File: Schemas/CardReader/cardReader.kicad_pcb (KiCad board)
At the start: 2 copper layers, 50.2 x 56.5 mm, 29 parts, among them P1 PWR, P2 DATA, Q1 BC817-40, U1 74HC165

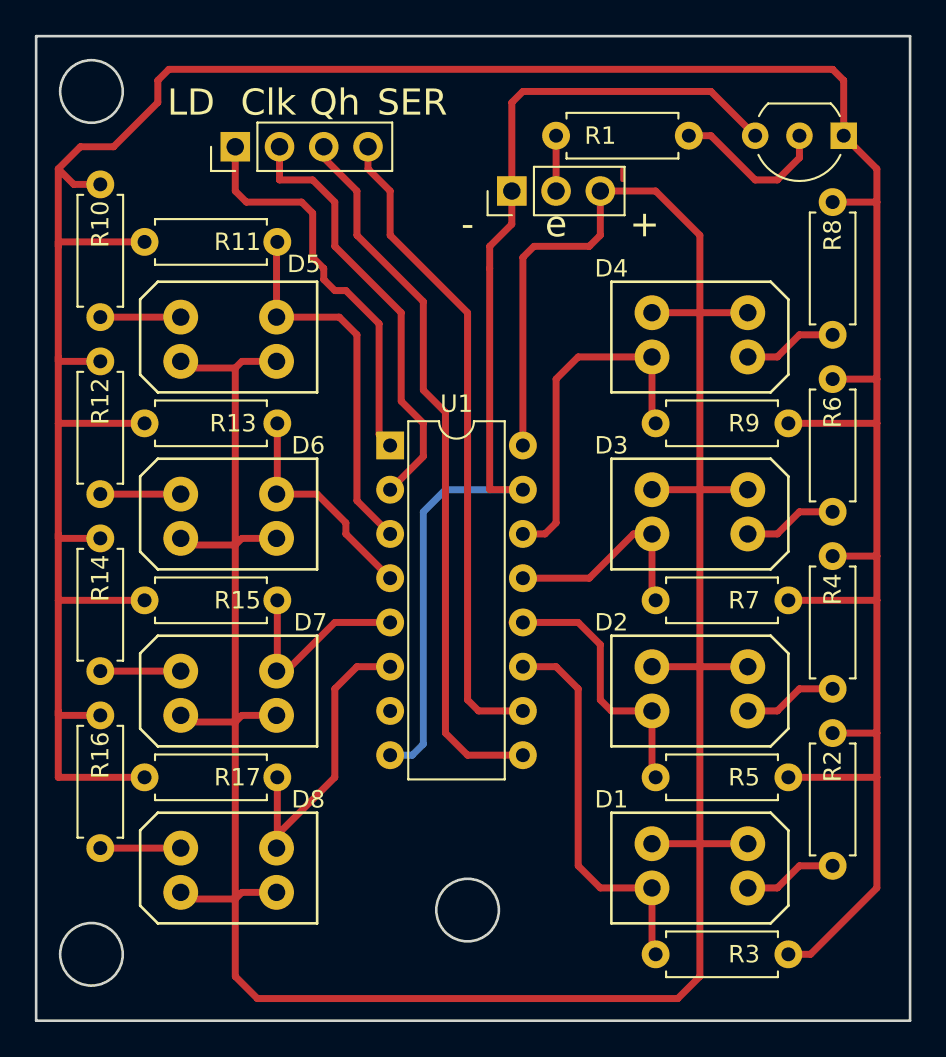
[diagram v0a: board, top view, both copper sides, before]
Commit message: Update cardReader schema, add end pin
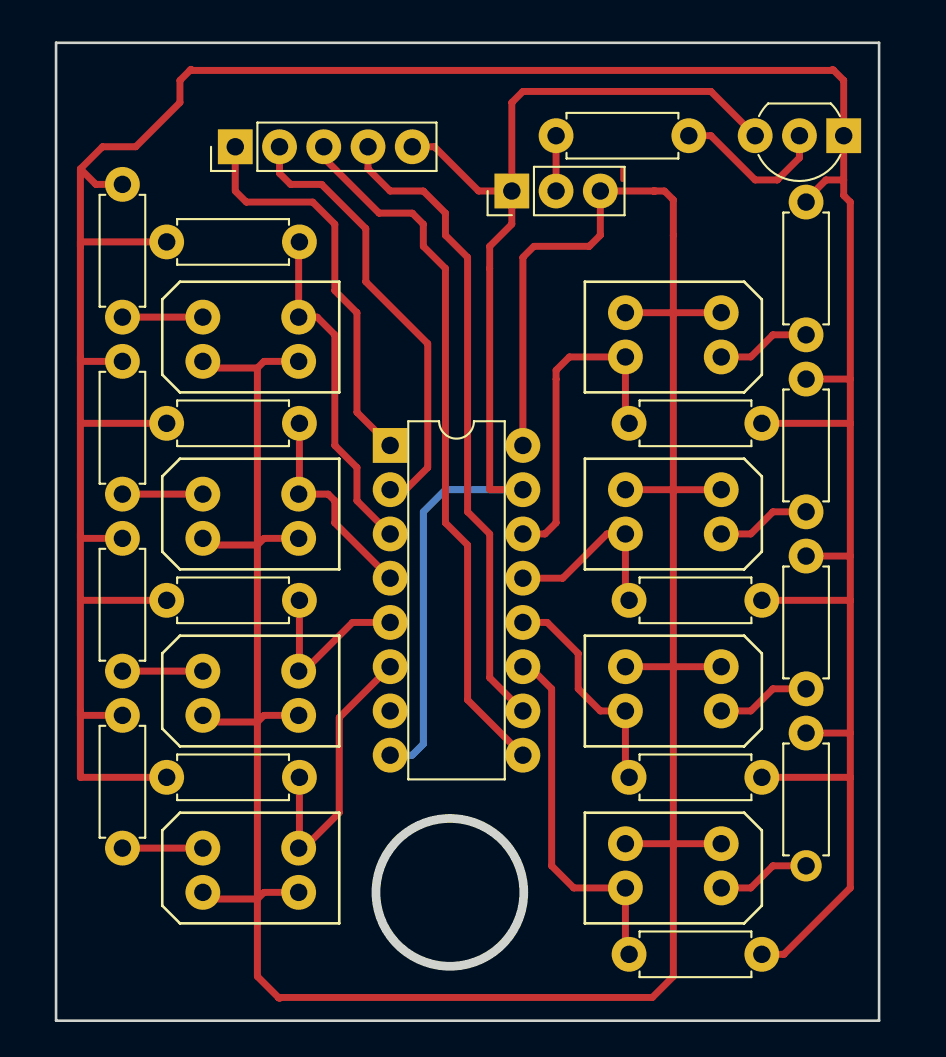
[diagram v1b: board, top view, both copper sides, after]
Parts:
- P2: footprint Pin_Headers:Pin_Header_Straight_1x04_Pitch2.54mm -> Pin_Headers:Pin_Header_Straight_1x05_Pitch2.54mm
- moved D1 1.52 mm to (145.2, 94.0)
- moved D2 1.52 mm to (145.2, 83.8)
- moved D3 1.52 mm to (145.2, 73.7)
- moved D4 1.52 mm to (145.2, 63.5)
- moved R2 1.52 mm to (152.8, 86.4)
- moved R4 1.52 mm to (152.8, 76.2)
- moved R6 1.52 mm to (152.8, 66.0)
- moved R8 1.52 mm to (152.8, 55.9)
- moved R3 1.52 mm to (150.2, 99.1)
- moved R5 1.52 mm to (150.2, 88.9)
- moved R7 1.52 mm to (150.2, 78.7)
- moved R9 1.52 mm to (150.2, 68.6)
- moved D5 1.27 mm to (120.9, 63.8)
- moved D6 1.27 mm to (120.9, 73.9)
- moved D7 1.27 mm to (120.9, 84.1)
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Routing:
- net /gnd: track 61.7 -> 68.5 mm
- net /pwr: track 175.5 -> 172.6 mm
- net Net-(D2-Pad4): track 15.9 -> 13.1 mm
- net Net-(D5-Pad4): track 21.6 -> 19.6 mm
- net Net-(D1-Pad4): track 22.5 -> 20.6 mm
- net Net-(D3-Pad4): track 12.4 -> 10.8 mm
- net Net-(Q1-Pad1): track 193.4 -> 192.0 mm
- net Net-(D4-Pad4): track 21.0 -> 19.8 mm
- net Net-(D6-Pad4): track 13.0 -> 12.1 mm
- net /SH/LD: track 23.1 -> 24.0 mm
- net Net-(D8-Pad4): track 18.3 -> 17.6 mm
- net /Qh: track 41.5 -> 40.8 mm
- net Net-(D7-Pad4): track 11.8 -> 11.0 mm
- net /CLK: track 25.0 -> 25.7 mm
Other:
- board size 50.2 x 56.5 mm -> 47.2 x 56.1 mm
- net class Default: via_dia 0.6 -> 1.2; via_drill 0.4 -> 1
- board text added: "end"

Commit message: minor updates to cardReader schema
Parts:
- moved R5 99.2 mm to (56.3, 57.1)
- moved D1 99.2 mm to (51.2, 62.2)
- moved D3 99.2 mm to (51.2, 41.9)
- moved D4 99.2 mm to (51.2, 31.8)
- moved P2 99.2 mm to (26.0, 21.0)
- moved R1 99.2 mm to (44.5, 20.3)
- moved R13 99.2 mm to (22.1, 36.8)
- moved R17 99.2 mm to (22.1, 57.1)
- moved R2 99.2 mm to (58.8, 54.6)
- moved R3 99.2 mm to (56.3, 67.3)
- moved R4 99.2 mm to (58.8, 44.5)
- moved R6 99.2 mm to (58.8, 34.3)
- moved R7 99.2 mm to (56.3, 47.0)
- moved R8 99.2 mm to (58.8, 24.1)
- moved R9 99.2 mm to (56.3, 36.8)
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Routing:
- net (no net): track 0.63 -> 0.00 mm
